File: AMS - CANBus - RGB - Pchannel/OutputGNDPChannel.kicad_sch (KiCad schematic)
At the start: 16 parts, among them Q2 IRF510, Q3 IRF510, Q4 IRF510, Q5 IRF510

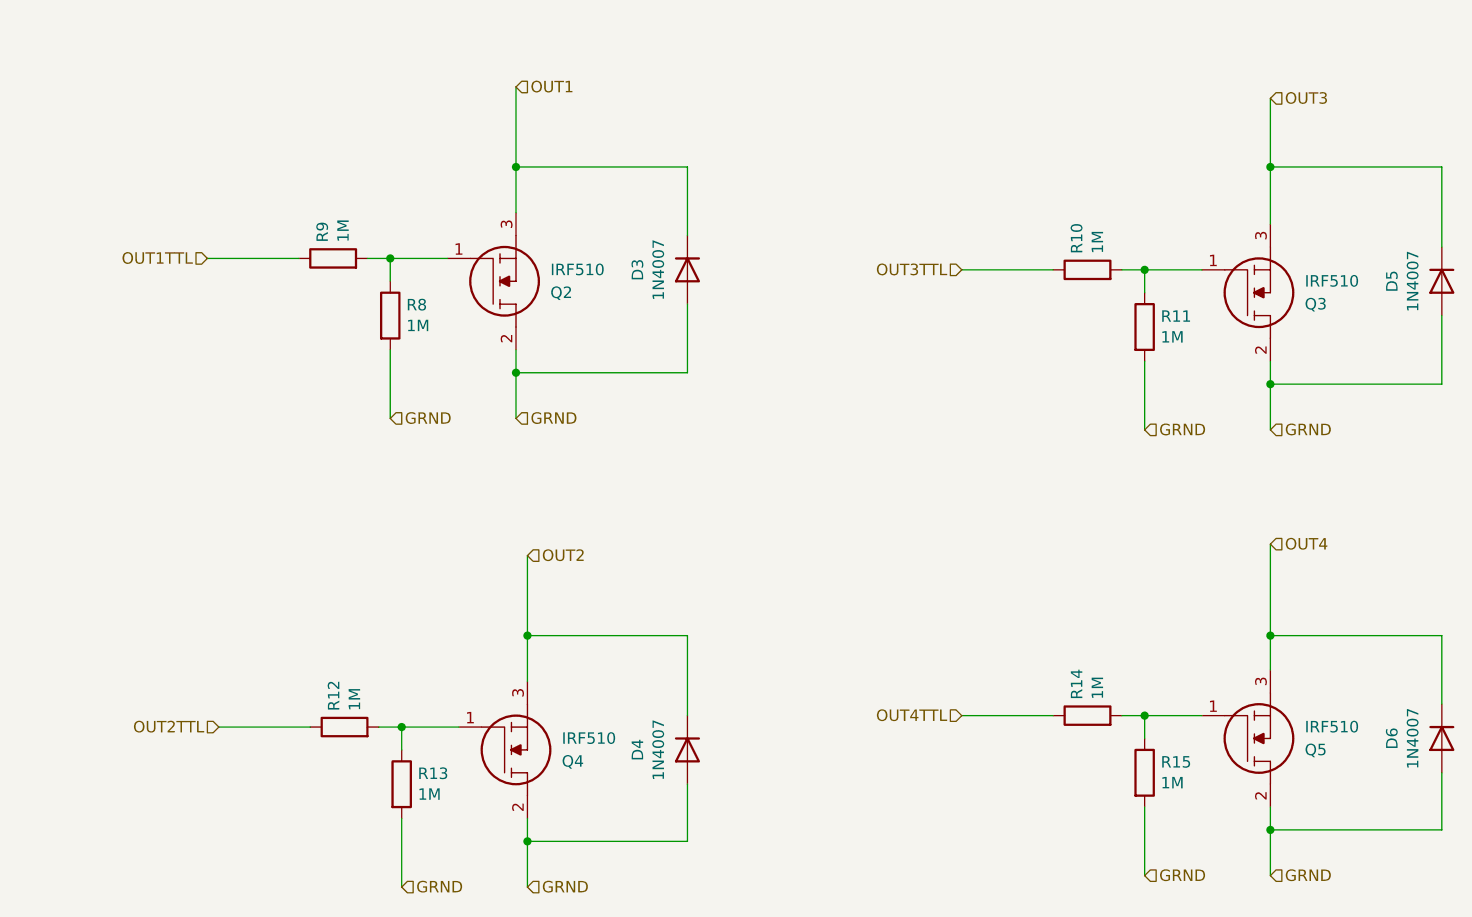
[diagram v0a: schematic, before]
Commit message: initial change from a bad low side switch to a high side switch
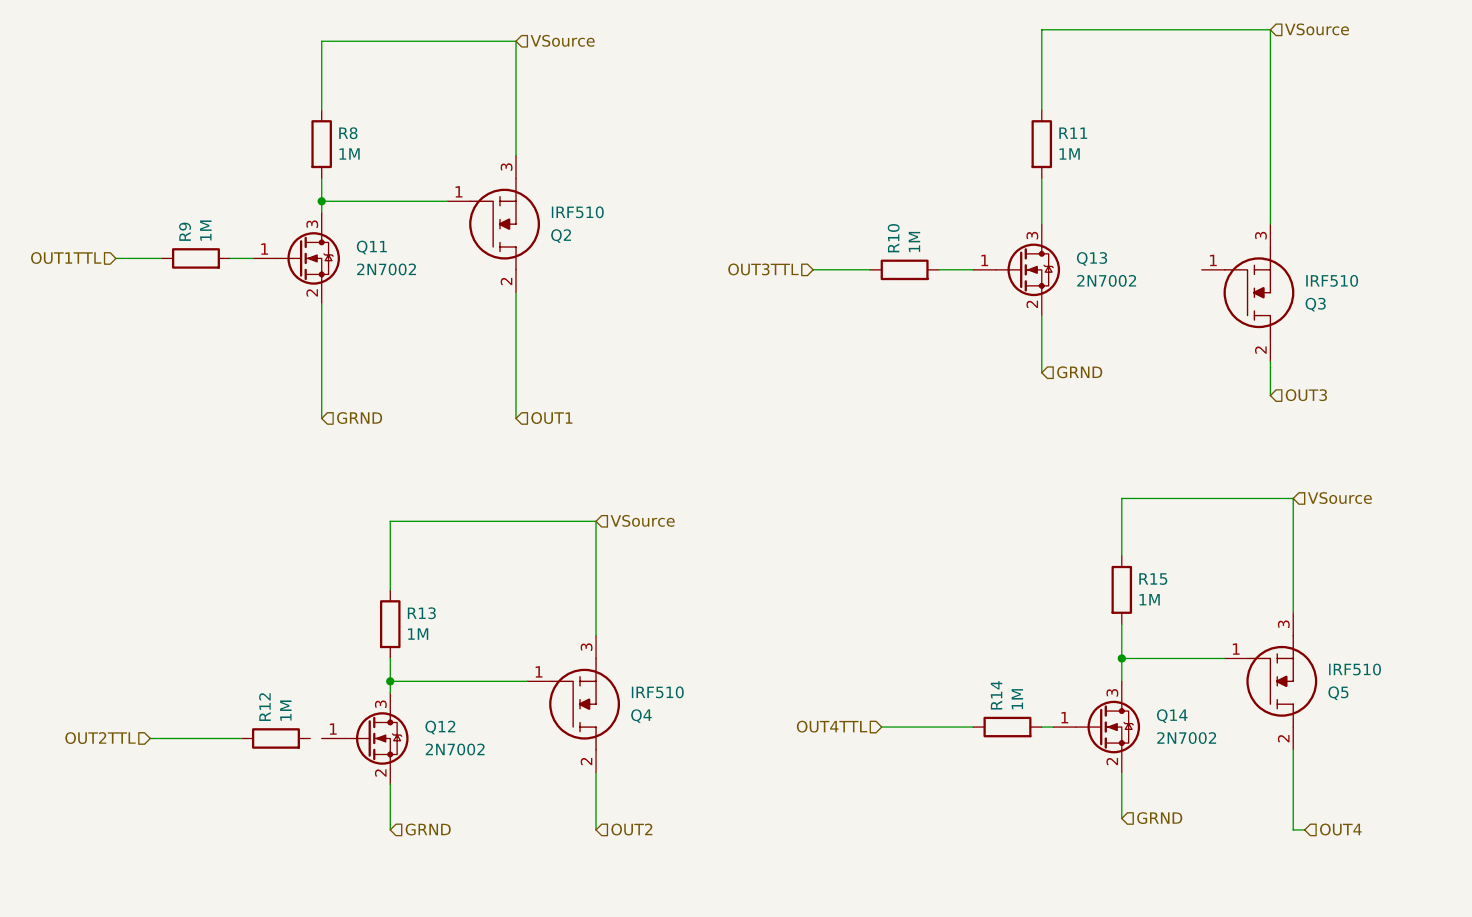
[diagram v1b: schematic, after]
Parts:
- removed D3, D4, D5, D6: 1N4007, Diode_THT:D_DO-41_SOD81_P10.16mm_Horizontal, symbol Diode:1N4007
- added Q11, Q12, Q13, Q14: 2N7002, Package_TO_SOT_SMD:SOT-23, symbol Transistor_FET:2N7002
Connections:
- net GRND: now also Q11.2 (S), Q12.2 (S), Q13.2 (S), Q14.2 (S); no longer Q2.2, Q3.2, Q4.2, Q5.2, R11.2, R13.2, R15.2, R8.2
- net OUT1: now also Q2.2; no longer Q2.3
- net OUT2: now also Q4.2; no longer Q4.3
- net OUT3: now also Q3.2; no longer Q3.3
- net OUT4: now also Q5.2; no longer Q5.3
- new net: Q14.3 (D), Q5.1, R15.2
- new net: Q11.3 (D), Q2.1, R8.2
- new net: Q13.1 (G), R10.2
- new net: Q11.1 (G), R9.2
- new net: Q14.1 (G), R14.2
- new net: Q13.3 (D), R11.2
- new net: Q12.3 (D), Q4.1, R13.2
- new net VSource: Q2.3, Q3.3, Q4.3, Q5.3, R11.1, R13.1, R15.1, R8.1
- now unconnected: Q3.1, R12.2
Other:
- moved on the sheet: Q2, Q4, Q5, R10, R11, R12, R13, R14, R15, R8, R9

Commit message: wip
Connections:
- net OUT1: no longer Q2.2
- net OUT2: no longer Q4.2
- net OUT3: no longer Q3.2
- net OUT4: no longer Q5.2
- net at R11.2: no longer Q13.3 (D)
- removed net VSource: Q2.3, Q3.3, Q4.3, Q5.3, R11.1, R13.1, R15.1, R8.1
- now unconnected: Q11.3 (D), Q12.3 (D), Q14.3 (D), Q2.1, Q4.1, Q5.1, R13.2, R15.2, R8.2
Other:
- moved on the sheet: Q2, Q3, Q4, Q5
